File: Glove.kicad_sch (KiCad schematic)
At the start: 41 parts, among them J1 USB_C_Receptacle_USB2.0, J2 Joystick, Q1 2N7002, Q2 2N7002, U1 LM1117-3.3, U2 ESP32-WROOM-32D, U3 CP2102N-Axx-xQFN24

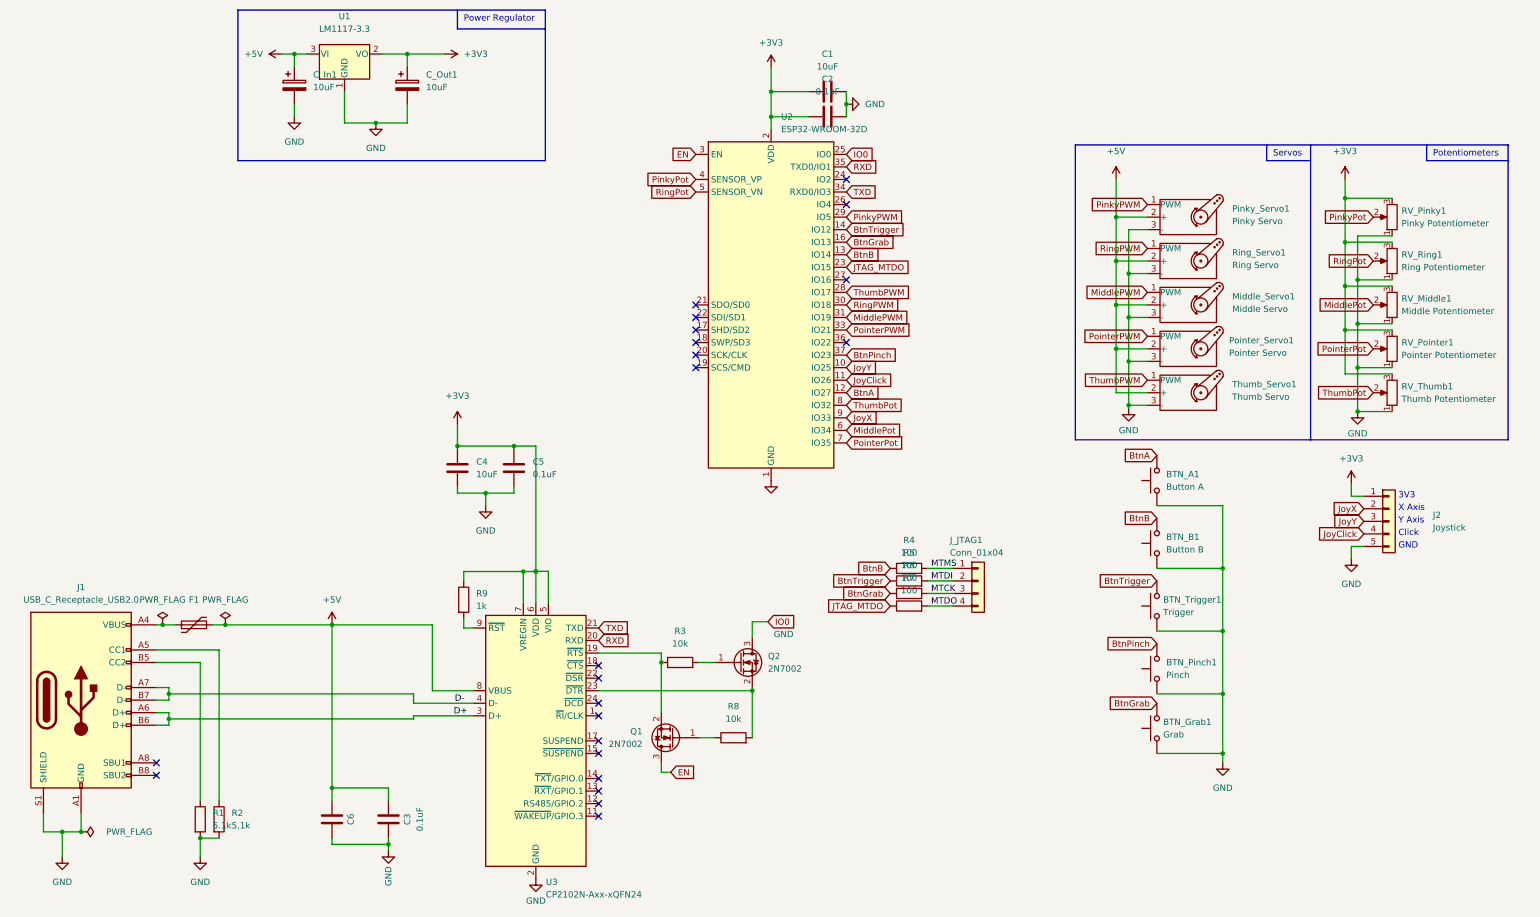
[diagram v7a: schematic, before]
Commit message: Connect all servos and potentiometers in parallel
This saves a bunch of board space.

Signed-off-by: Kozova1 <mug66kk@gmail.com>
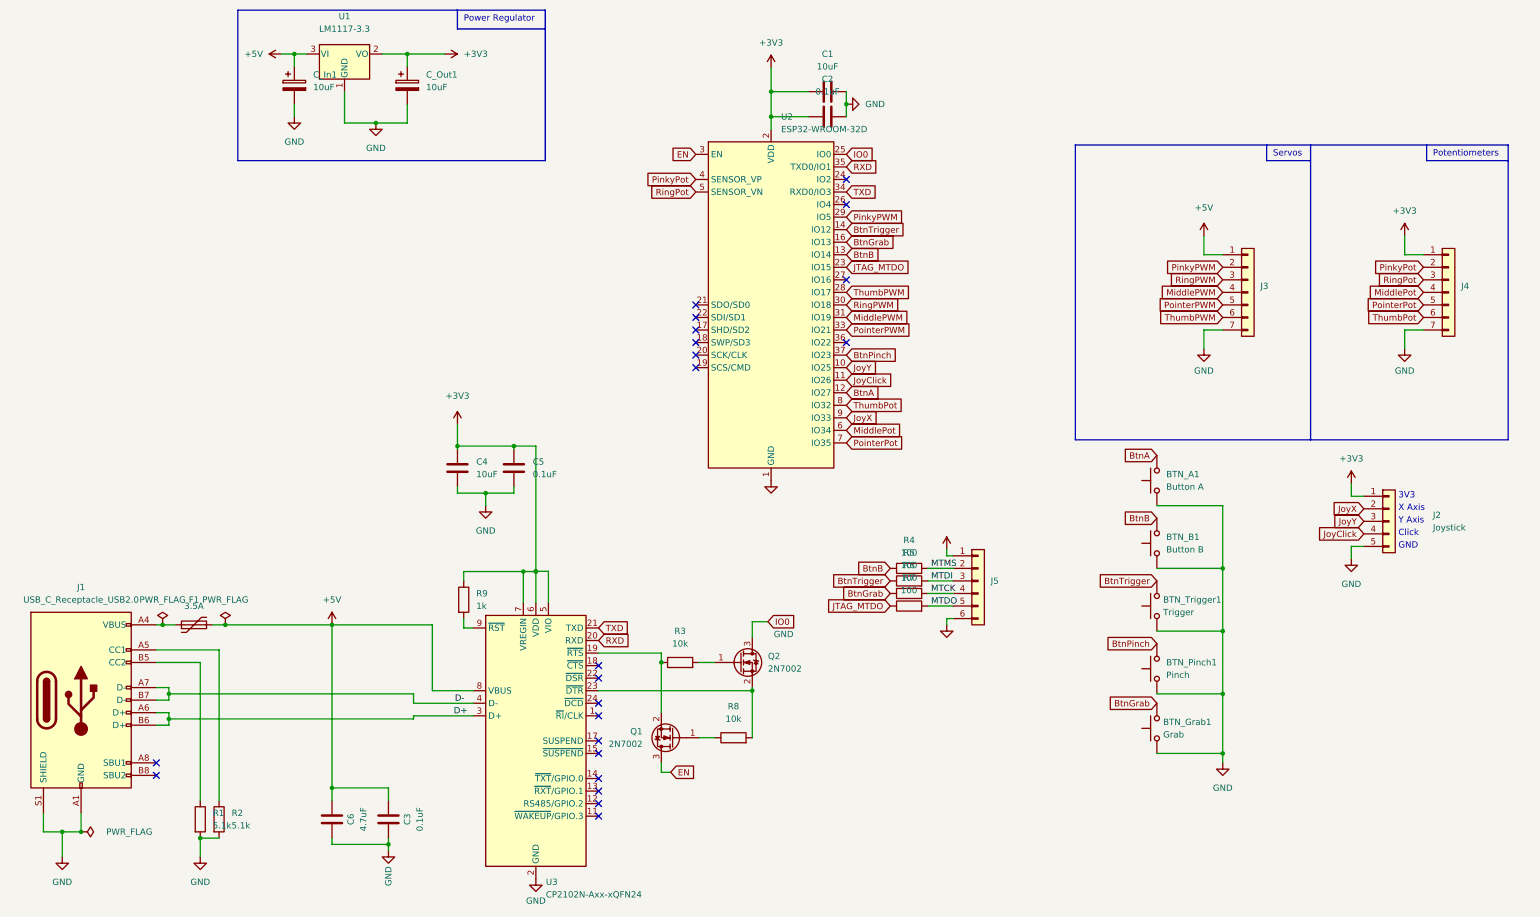
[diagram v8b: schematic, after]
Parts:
- removed J_JTAG1: Conn_01x04, Connector_PinHeader_2.54mm:PinHeader_1x04_P2.54mm_Vertical, symbol Connector_Generic:Conn_01x04
- removed Middle_Servo1: Middle Servo, Connector_JST:JST_XH_B3B-XH-A_1x03_P2.50mm_Vertical, symbol Motor:Motor_Servo
- removed Pinky_Servo1: Pinky Servo, Connector_JST:JST_XH_B3B-XH-A_1x03_P2.50mm_Vertical, symbol Motor:Motor_Servo
- removed Pointer_Servo1: Pointer Servo, Connector_JST:JST_XH_B3B-XH-A_1x03_P2.50mm_Vertical, symbol Motor:Motor_Servo
- removed RV_Middle1: Middle Potentiometer, Connector_JST:JST_XH_B3B-XH-A_1x03_P2.50mm_Vertical, symbol Device:R_Potentiometer
- removed RV_Pinky1: Pinky Potentiometer, Connector_JST:JST_XH_B3B-XH-A_1x03_P2.50mm_Vertical, symbol Device:R_Potentiometer
- removed RV_Pointer1: Pointer Potentiometer, Connector_JST:JST_XH_B3B-XH-A_1x03_P2.50mm_Vertical, symbol Device:R_Potentiometer
- removed RV_Ring1: Ring Potentiometer, Connector_JST:JST_XH_B3B-XH-A_1x03_P2.50mm_Vertical, symbol Device:R_Potentiometer
- removed RV_Thumb1: Thumb Potentiometer, Connector_JST:JST_XH_B3B-XH-A_1x03_P2.50mm_Vertical, symbol Device:R_Potentiometer
- removed Ring_Servo1: Ring Servo, Connector_JST:JST_XH_B3B-XH-A_1x03_P2.50mm_Vertical, symbol Motor:Motor_Servo
- removed Thumb_Servo1: Thumb Servo, Connector_JST:JST_XH_B3B-XH-A_1x03_P2.50mm_Vertical, symbol Motor:Motor_Servo
- added J3, J4: (no value), symbol Connector_Generic:Conn_01x07
- added J5: (no value), symbol Connector_Generic:Conn_01x06
- C6: value (none) -> 4.7uF; footprint (none) -> Capacitor_SMD:C_0805_2012Metric_Pad1.18x1.45mm_HandSolder
- F1: value (none) -> 3.5A; footprint (none) -> Fuse:Fuse_1812_4532Metric_Pad1.30x3.40mm_HandSolder
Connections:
- net +3V3: now also J4.1 (Pin_1), J5.1 (Pin_1)
- net +5V: now also J3.1 (Pin_1)
- net GND: now also J3.7 (Pin_7), J4.7 (Pin_7), J5.6 (Pin_6)
- net MTCK: now also J5.4 (Pin_4)
- net MTDI: now also J5.3 (Pin_3)
- net MTDO: now also J5.5 (Pin_5)
- net MTMS: now also J5.2 (Pin_2)
- net MiddlePWM: now also J3.4 (Pin_4)
- net MiddlePot: now also J4.4 (Pin_4)
- net PinkyPWM: now also J3.2 (Pin_2)
- net PinkyPot: now also J4.2 (Pin_2)
- net PointerPWM: now also J3.5 (Pin_5)
- net PointerPot: now also J4.5 (Pin_5)
- net RingPWM: now also J3.3 (Pin_3)
- net RingPot: now also J4.3 (Pin_3)
- net ThumbPWM: now also J3.6 (Pin_6)
- net ThumbPot: now also J4.6 (Pin_6)
